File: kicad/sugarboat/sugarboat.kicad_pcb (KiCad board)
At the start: 2 copper layers, 34 x 132 mm, 52 parts, among them IC1 DW01A, J1 TYPE-C-31-M-12, Q1 FS8205A, Q2 AO3401A, U1 TP4056, U2 MPU-6050, U3 HT7330, U4 E73-2G4M08S1C, U5 SHT30-DIS, Y1 32.768 kHz

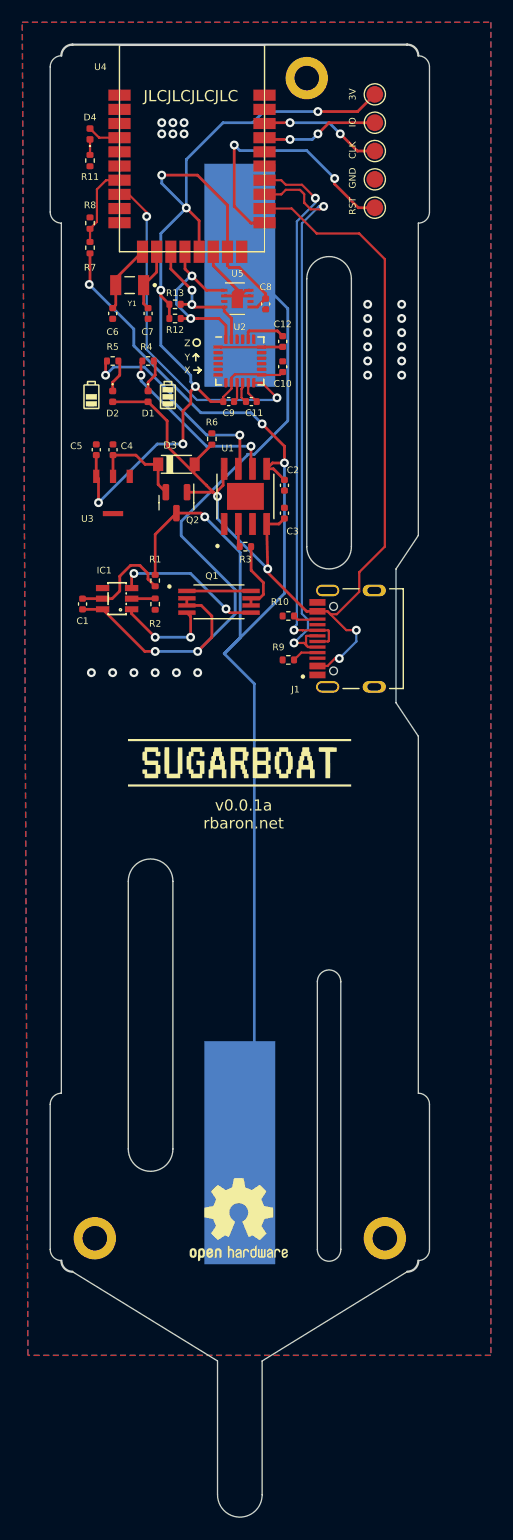
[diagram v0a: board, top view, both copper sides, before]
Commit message: Renamed KiCad project to sugarboat
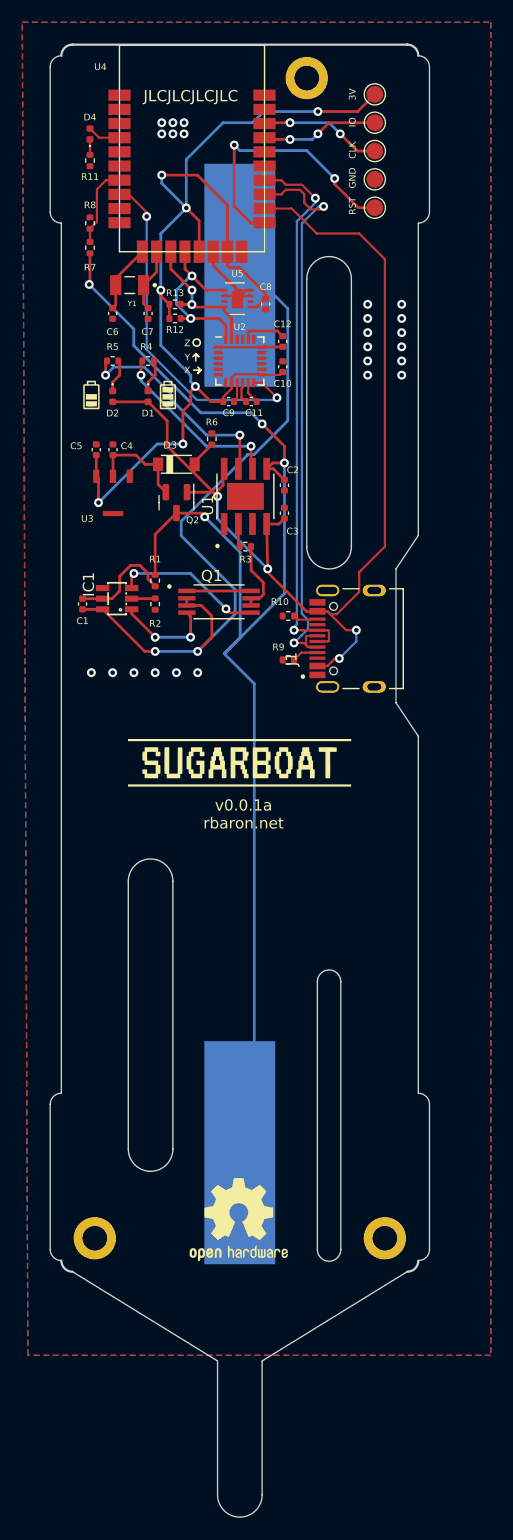
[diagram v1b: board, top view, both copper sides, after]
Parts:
- D3: value B5819W-TP -> B5819W SL

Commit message: Updates license to CC BY-NC-ND 4.0
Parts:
- removed the REF** at (112.9, 163.3)
